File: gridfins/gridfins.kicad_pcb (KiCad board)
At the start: 4 copper layers, 47.1 x 85.5 mm, 207 parts, among them IC1 2536030320001, J1 RBUS, J10 Limit switch 2, J11 Conn_01x03_Pin, J2 USB_C_Receptacle_USB2.0, J3 ServoCH0, J4 ServoCH1, J5 ServoCH2, J6 ST1W008S4TR2000, J7 Encoder breakout, J8 1053131104, J9 Limit switch 1, Q1 SSM3K15AMFV,L3F, Q3 DMP3099, Q4 SSM3K15AMFV,L3F, Q5 BSZ025N04LS, Q6 BSZ025N04LS, U1 ESP32-S3, U10 LM74810, U12 SiC437AED-T1, U2 SN65HVD230, U3 LM66200DRLR, U4 MAX77827AEFD+T, U5 SC4215ASTRT, U6 SiC437AED-T1, U7 DRV8834PWP, U8 MMC5983MA, U9 H3LIS331DLTR, Y1 R940000171

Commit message: formatting
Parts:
- removed R58, R60: 10k, Resistor_SMD:R_0402_1005Metric
- removed R59: 113k, Resistor_SMD:R_0402_1005Metric
- removed R63: 442k, Resistor_SMD:R_0402_1005Metric
- added R401: 10kΩ, Resistor_SMD:R_0402_1005Metric, F.Cu at (245.4, 75.1)
- added R402: 113kΩ, Resistor_SMD:R_0402_1005Metric, F.Cu at (246.2, 70.2)
- added R403: 10kΩ, Resistor_SMD:R_0402_1005Metric, F.Cu at (245.2, 72.8)
- added R406: 442kΩ, Resistor_SMD:R_0402_1005Metric, F.Cu at (246.2, 68.7)
- C103: renamed from C8; value 0.1uF -> 100nF
- C105: renamed from C5; value 0.1uF -> 100nF
- C106: renamed from C6; value 0.1uF -> 100nF
- C109: renamed from C10; value 0.1uF -> 100nF
- C110: renamed from C3; value 0.1uF -> 100nF
- C1102: renamed from C19; value 0.01uF -> 10nF
- C1103: renamed from C56; value 0.01uF -> 10nF
- C1104: renamed from C28; value 0.1uF -> 100nF
- C111: renamed from C11; value 0.1uF -> 100nF
- C114: renamed from C45; value 0.1uF -> 100nF
- C208: renamed from C27; value 0.1uF -> 100nF
- C301: renamed from C52; value 0.1uF -> 100nF
- C303: renamed from C54; value 0.1uF -> 100nF
- C304: renamed from C55; value 0.1uF -> 100nF
- C410: renamed from C89; value 0.1uF -> 100nF
- C510: renamed from C64; value 0.1uF -> 100nF
- C801: renamed from C51; value 0.1uF -> 100nF
- L101: renamed from L1; value 2.0nH -> 2nH
- LED101: renamed from LED1; value GREEN_LED -> LED_GREEN
- LED102: renamed from LED2; value GREEN_LED -> LED_GREEN
- LED103: renamed from LED3; value ORANGE_LED -> LED_ORANGE
- LED104: renamed from LED4; value BLUE_LED -> LED_BLUE
- LED105: renamed from LED5; value RED_LED -> LED_RED
- LED601: renamed from LED6; value WHITE_LED -> LED_WHITE
- R1001: renamed from R25; value 165R -> 165Ω
- R1002: renamed from R26; value 165R -> 165Ω
- R1003: renamed from R27; value 165R -> 165Ω
- R101: renamed from R1; value 10K -> 10kΩ
- R102: renamed from R2; value 470 -> 470Ω
- R103: renamed from R5; value 1k -> 1kΩ
- R104: renamed from R18; value 1k -> 1kΩ
- R105: renamed from R3; value 10K -> 10kΩ
- R106: renamed from R4; value 470 -> 470Ω
- R107: renamed from R6; value 499R -> 499Ω
- R108: renamed from R7; value 3k -> 3kΩ
- R109: renamed from R49; value 10k -> 10kΩ
- R110: renamed from R36; value 1.5k -> 1.5kΩ
- R1101: renamed from R47; value 10k -> 10kΩ
- R1102: renamed from R40; value 51K -> 51kΩ
- R1103: renamed from R41; value 51K -> 51kΩ
- R1104: renamed from R46; value 10k -> 10kΩ
- R1105: renamed from R43; value 0.5 -> 0.5Ω
- R1106: renamed from R44; value 0.5 -> 0.5Ω
- R111: renamed from R37; value 470 -> 470Ω
- R112: renamed from R48; value 10k -> 10kΩ
- R113: renamed from R34; value 18k -> 18kΩ
- R114: renamed from R45; value 18k -> 18kΩ
- R201: renamed from R14; value 10k -> 10kΩ
- R202: renamed from R15; value 14k -> 14kΩ
- R203: renamed from R16; value 56k -> 56kΩ
- R204: renamed from R17; value 10k -> 10kΩ
- R301: renamed from R31; value 10k -> 10kΩ
- R302: renamed from R32; value 100k -> 100kΩ
- R303: renamed from R33; value 5.1k -> 5.1kΩ
- R304: renamed from R35; value 4.22k -> 4.22kΩ
- R404: renamed from R61; value 2.2 -> 2.2Ω
- R405: renamed from R62; value 1k -> 1kΩ
- R407: renamed from R64; value 200k -> 200kΩ
- R408: renamed from R65; value 100k -> 100kΩ
- R409: renamed from R66; value 10k -> 10kΩ
- R410: renamed from R67; value 5.1R -> 5.1Ω
- R501: renamed from R20; value 10k -> 10kΩ
- R502: renamed from R21; value 157k -> 157kΩ
- R503: renamed from R22; value 10k -> 10kΩ
- R504: renamed from R23; value 2.2 -> 2.2Ω
- R505: renamed from R24; value 1k -> 1kΩ
- R506: renamed from R38; value 0 -> 0Ω
- R507: renamed from R39; value 200k -> 200kΩ
- R508: renamed from R42; value 100k -> 100kΩ
- R509: renamed from R56; value 10k -> 10kΩ
- R510: renamed from R57; value 5.1R -> 5.1Ω
- R601: renamed from R11; value 5.1k -> 5.1kΩ
- R602: renamed from R12; value 5.1k -> 5.1kΩ
- R603: renamed from R13; value 5.1k -> 5.1kΩ
- R701: renamed from R8; value 0 -> 0Ω
- R702: renamed from R9; value 60 -> 60Ω
- R703: renamed from R10; value 60 -> 60Ω
- R801: renamed from R71; value 1k -> 1kΩ
- R802: renamed from R30; value 10k -> 10kΩ
- renumbered C1 to C101, C2 to C102, C4 to C104, C7 to C107, C9 to C108, C57 to C1101, C29 to C1105, C30 to C1106, C13 to C112, C14 to C113, C20 to C201, C21 to C202, C22 to C203, C23 to C204, C24 to C205, C25 to C206, C26 to C207, C53 to C302, C80 to C401, C81 to C402, C82 to C403, C83 to C404, C84 to C405, C85 to C406, C87 to C407, C88 to C408, C86 to C409, C90 to C411, C91 to C412, C92 to C413, C93 to C414, C96 to C415, C95 to C416, C94 to C417, C38 to C501, C39 to C502, C40 to C503, C46 to C504, C47 to C505, C48 to C506, C49 to C507, C61 to C508, C62 to C509, C65 to C511, C66 to C512, C75 to C513, C76 to C514, C77 to C515, C78 to C516, C79 to C517, C15 to C701, C16 to C702, C17 to C703, C12 to C901, C34 to C902, C36 to C903, C41 to C904, C42 to C905, C44 to C906, C50 to C907, D3 to D1001, D5 to D1002, D4 to D1003, D2 to D601, D1 to D701, H1 to H101, H2 to H102, H3 to H103, H4 to H104, J3 to J1001, J4 to J1002, J5 to J1003, J11 to J101, J1 to J102, J10 to J103, J9 to J104, J7 to J105, J8 to J1101, J2 to J601, J6 to J801, JP1 to JP701, JP34 to JP801, L2 to L102, L3 to L201, L6 to L401, L4 to L501, Q5 to Q301, Q6 to Q302, Q4 to Q401, Q1 to Q501, Q3 to Q801, TP9 to TP101, TP10 to TP102, TP25 to TP103, TP26 to TP104, TP27 to TP105, TP7 to TP106, TP14 to TP107, TP11 to TP108, TP13 to TP109, TP12 to TP1101, TP4 to TP201, TP5 to TP202, TP6 to TP203, TP8 to TP204, TP1 to TP601, TP2 to TP602, U1 to U101, U7 to U1101, U3 to U201, U4 to U202, U5 to U203, U10 to U301, U12 to U401, U6 to U501, U2 to U701, U9 to U901, IC1 to U902, U8 to U903, Y1 to Y101

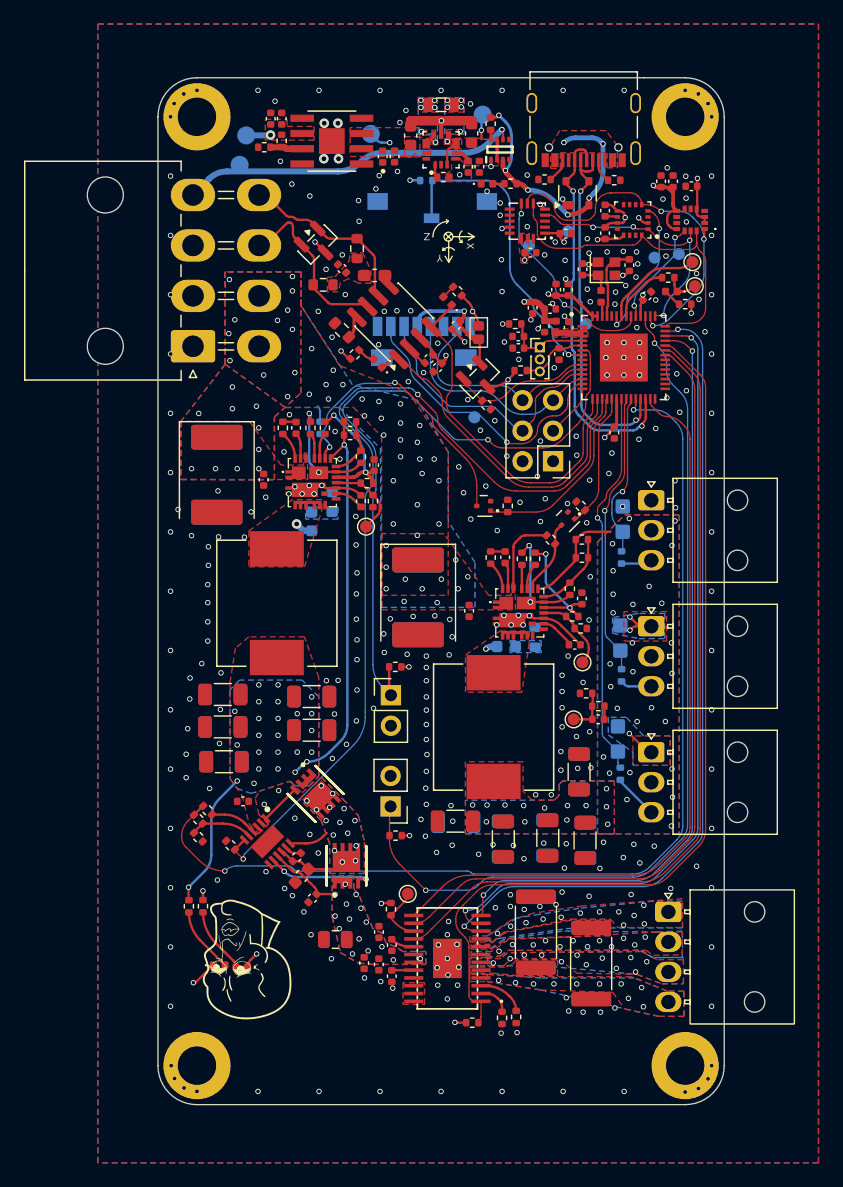
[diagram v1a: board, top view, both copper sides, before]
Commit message: feat: Post Jack review
Changed buck inductors to be wuerth. Reduced board footprint. Incorporated review feedback
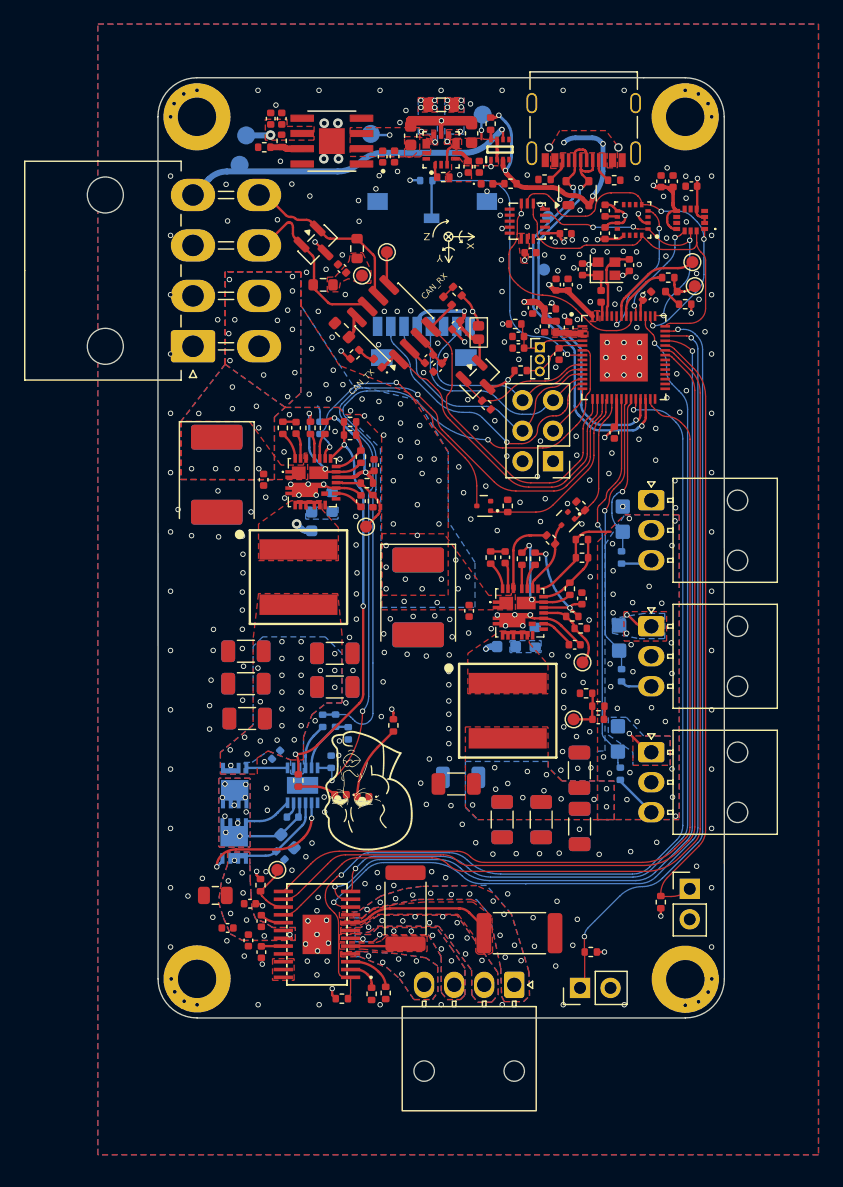
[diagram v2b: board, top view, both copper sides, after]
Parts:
- removed JP701: TermJP, Capacitor_SMD:C_0603_1608Metric_Pad1.08x0.95mm_HandSolder
- removed TP103, TP104, TP105, TP106: TestPoint, TestPoint:TestPoint_Pad_D1.0mm
- added TP701: TestPoint, TestPoint:TestPoint_Pad_D1.0mm, F.Cu at (227.9, 46.7)
- added TP702: TestPoint, TestPoint:TestPoint_Pad_D1.0mm, F.Cu at (230.0, 44.8)
- C301, C302, C303, C304, Q301, Q302, R301, R302, R303, R304, U301: moved to B.Cu
- L401, L501: footprint iclr:IND_SPM10065VT-3R3M-D -> iclr:WE-XHMI_7070
- moved J104 29.0 mm to (246.1, 106.0), turned to 90 degrees
- moved R112 28.8 mm to (247.0, 103.0)
- moved J103 25.8 mm to (255.2, 97.8), turned to 0 degrees
- moved R109 22.8 mm to (252.8, 98.9), turned to -90 degrees
- moved R106 21.9 mm to (230.5, 84.2)
- moved LED104 17.4 mm to (228.0, 90.1)
- moved LED105 17.4 mm to (226.1, 89.9), turned to 180 degrees
- moved G*** 17.3 mm to (228.5, 89.6)
- moved R304 15.2 mm to (226.8, 84.8), turned to 90 degrees
- moved J1101 14.2 mm to (240.6, 105.8), turned to -90 degrees
- moved R303 14.1 mm to (225.7, 83.8), turned to 90 degrees
- moved R108 13.9 mm to (222.6, 88.8)
- moved R302 12.1 mm to (224.6, 83.8), turned to 90 degrees
- moved C1105 11.7 mm to (216.7, 101.0), turned to 180 degrees
- moved C404 11.2 mm to (246.0, 87.9), turned to 90 degrees
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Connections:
- L401 pad 1: +7.4V -> /Buck_SERVO/SW
- L401 pad 2: /Buck_SERVO/SW -> +7.4V
- L501 pad 1: +10V -> /Buck_H_bridge/SW
- L501 pad 2: /Buck_H_bridge/SW -> +10V
- U101 pad 24: /BUS_VMON -> /NSLEEP
- U101 pad 38: /NSLEEP -> /Switch_1
- U101 pad 39: /DIR/BPHASE -> /STEP/BENBL
- U101 pad 40: /STEP/BENBL -> /NENBL/AENBL
- U101 pad 41: /NENBL/AENBL -> /Switch_2
- U101 pad 45: /Switch_1 -> /DIR/BPHASE
- U101 pad 6: /Switch_2 -> /BUS_VMON
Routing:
- net /BUS_VMON: track 87.2 -> 60.8 mm, vias 2 -> 1
- net /Switch_1: track 75.8 -> 51.3 mm, vias 2 -> 0
- net GND: track 297.3 -> 282.0 mm, vias 344 -> 332
- net Net-(U1101-BISEN): track 0.00 -> 12.5 mm
- net /DIR/BPHASE: track 63.8 -> 76.0 mm
- net /Fault: track 68.8 -> 79.5 mm
- net /M0/APHASE: track 63.4 -> 74.0 mm
- net /M1: track 67.2 -> 77.7 mm
- net +10V: track 44.6 -> 34.3 mm, vias 26 -> 28
- net /NENBL/AENBL: track 68.9 -> 78.9 mm
- net /HSIDE_EN: track 76.9 -> 66.9 mm, vias 2 -> 3
- net /STEP/BENBL: track 67.4 -> 77.2 mm
- net /NSLEEP: track 76.2 -> 82.4 mm, vias 0 -> 2
- net /Switch_2: track 57.5 -> 62.3 mm, vias 1 -> 2
- net Net-(U1101-AISEN): track 0.00 -> 4.62 mm
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- added copper zone on In2.Cu, net GND
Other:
- board size 47.1 x 85.5 mm -> 47.2 x 78.3 mm
- board text added: "GIGA C.H.A.D V1.0"
- board text removed: "GIGA CHAD V1.0"
- board text removed: "connect to Voutswitch via"
